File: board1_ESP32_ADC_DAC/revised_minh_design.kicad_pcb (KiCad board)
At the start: 4 copper layers, 94 x 39 mm, 31 parts, among them J1 Conn_01x03_Male, J2 Conn_01x08_Male, J3 Conn_01x08_Male, J4 Conn_01x08_Male, U1 ESP32-DevKit-C, U2 LM7805_TO220, U3 MCP1754S-3302xCB, U4 MCP1825S-3.3V, U5 MCP1501-33xSN, U6 MCP3464R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

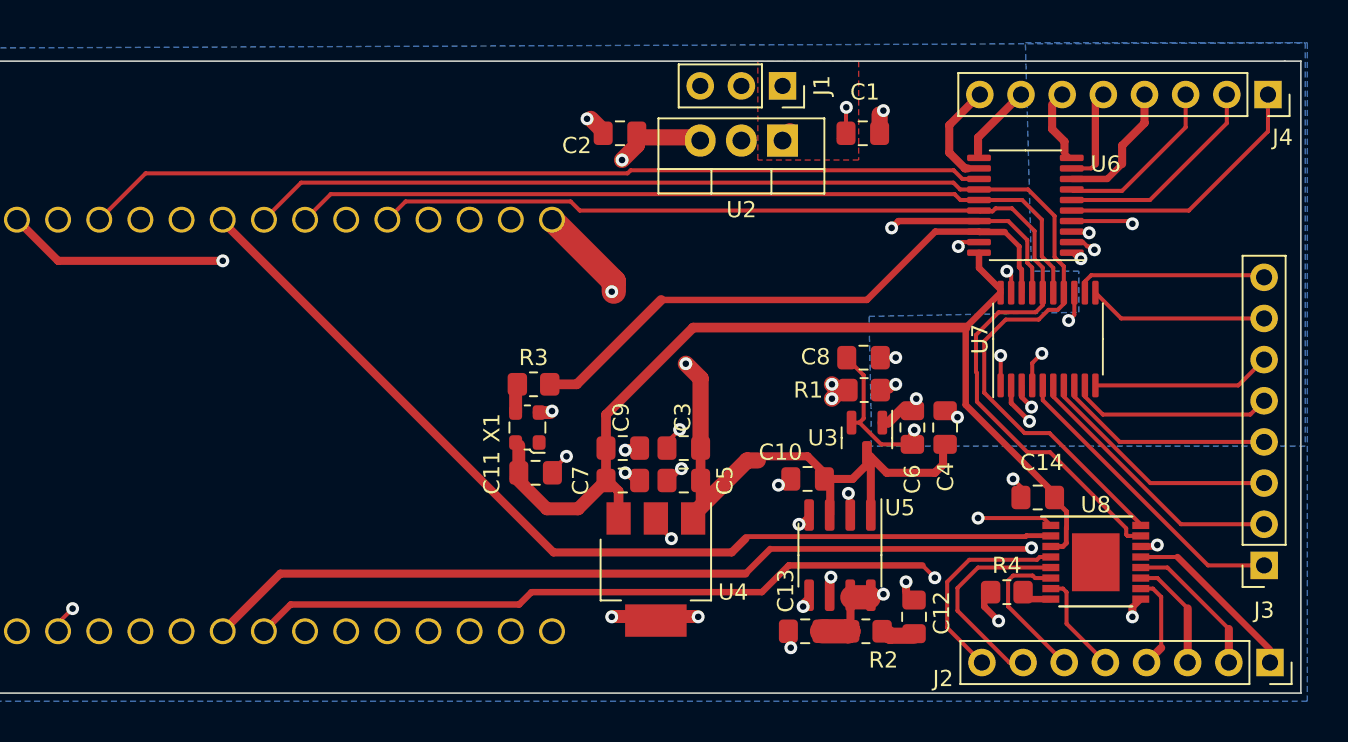
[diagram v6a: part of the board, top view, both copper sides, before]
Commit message: DAC ground to AGND, new AGND polygon pour
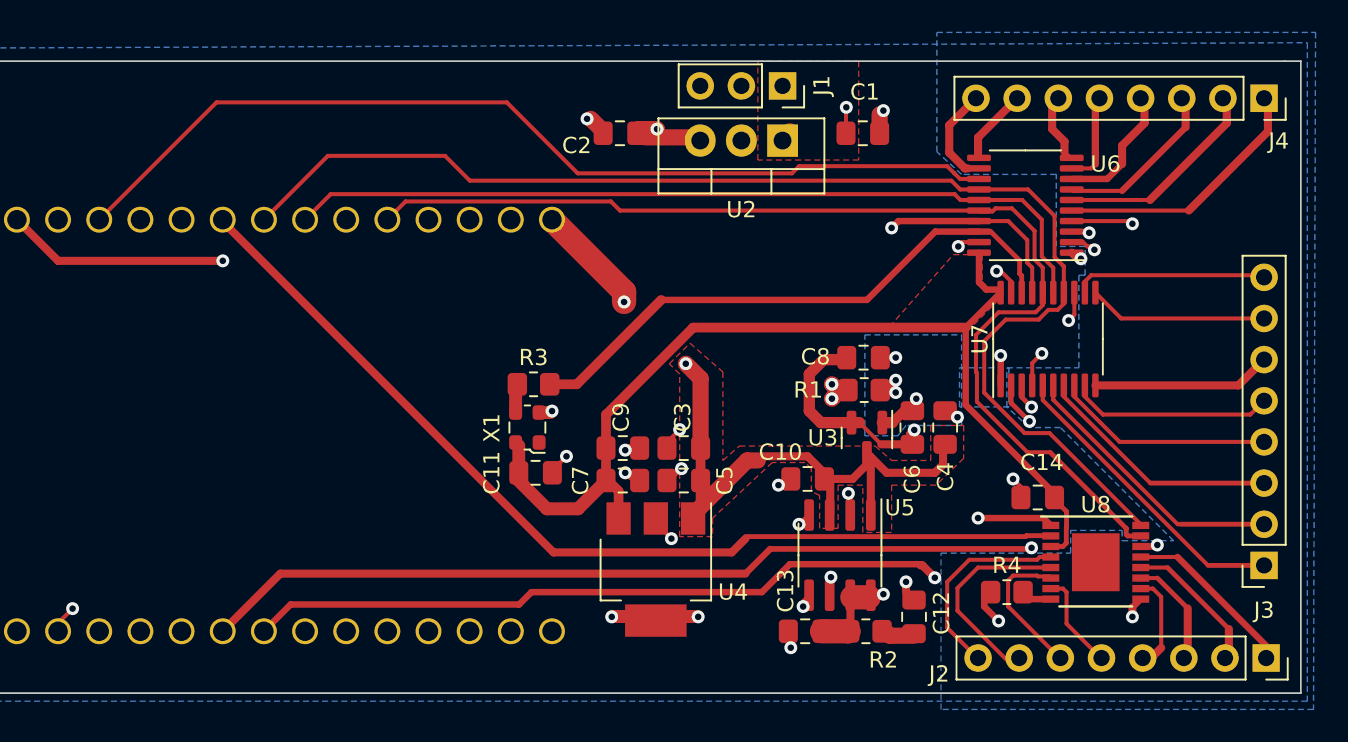
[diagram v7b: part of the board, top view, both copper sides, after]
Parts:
- moved J2 0.37 mm to (141.9, 76.8)
- moved J4 0.33 mm to (141.7, 42.3)
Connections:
- U8 pad 14: Earth -> GNDA
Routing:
- net ~{ADC1_CS}: track 55.8 -> 59.6 mm
- net +3.3VA: track 29.7 -> 33.4 mm
- net +5V: track 60.3 -> 63.9 mm
- net GNDA: track 13.4 -> 15.4 mm, vias 8 -> 10
- net SK: track 78.4 -> 79.8 mm
- net Earth: track 34.1 -> 33.4 mm, vias 25 -> 24
- net +3V3: track 62.5 -> 63.0 mm
- added copper zone on F.Cu, net +3V3
- added copper zone on F.Cu, net +5V

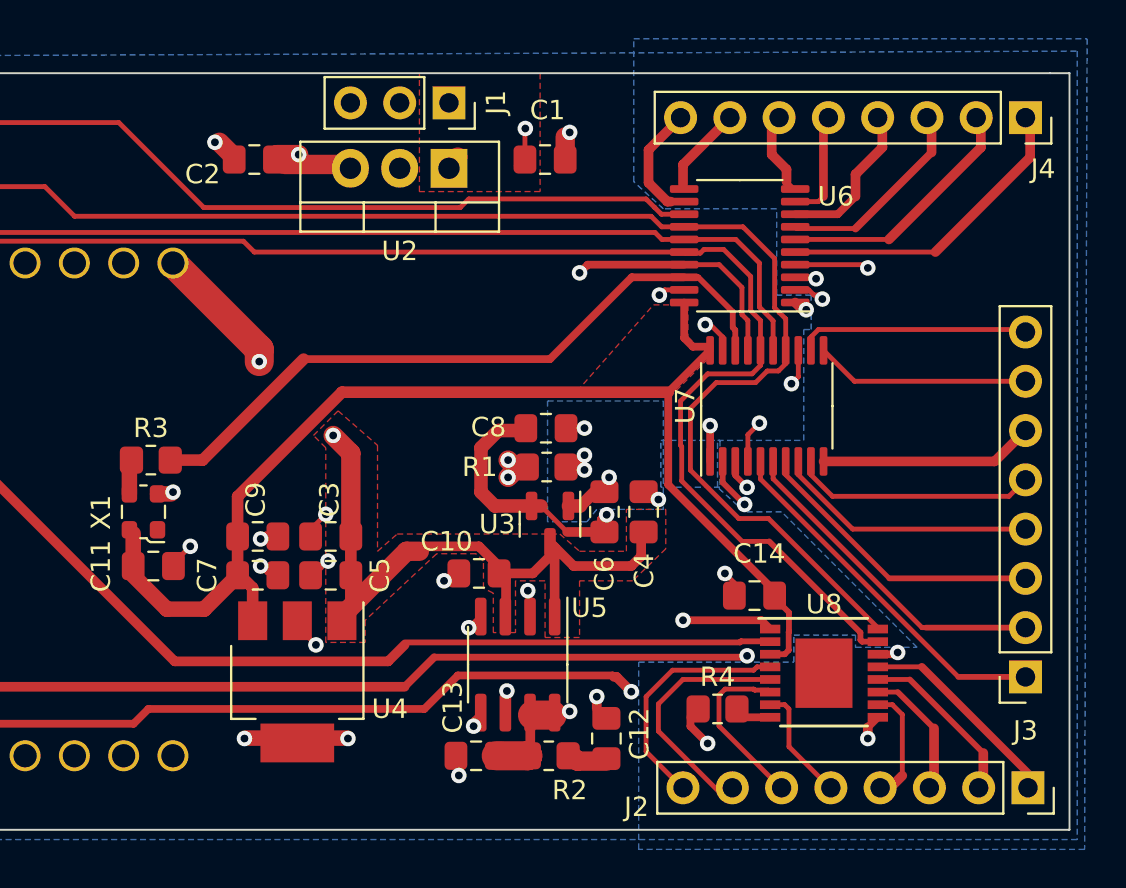
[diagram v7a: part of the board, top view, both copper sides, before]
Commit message: Split ground plane design with no errors
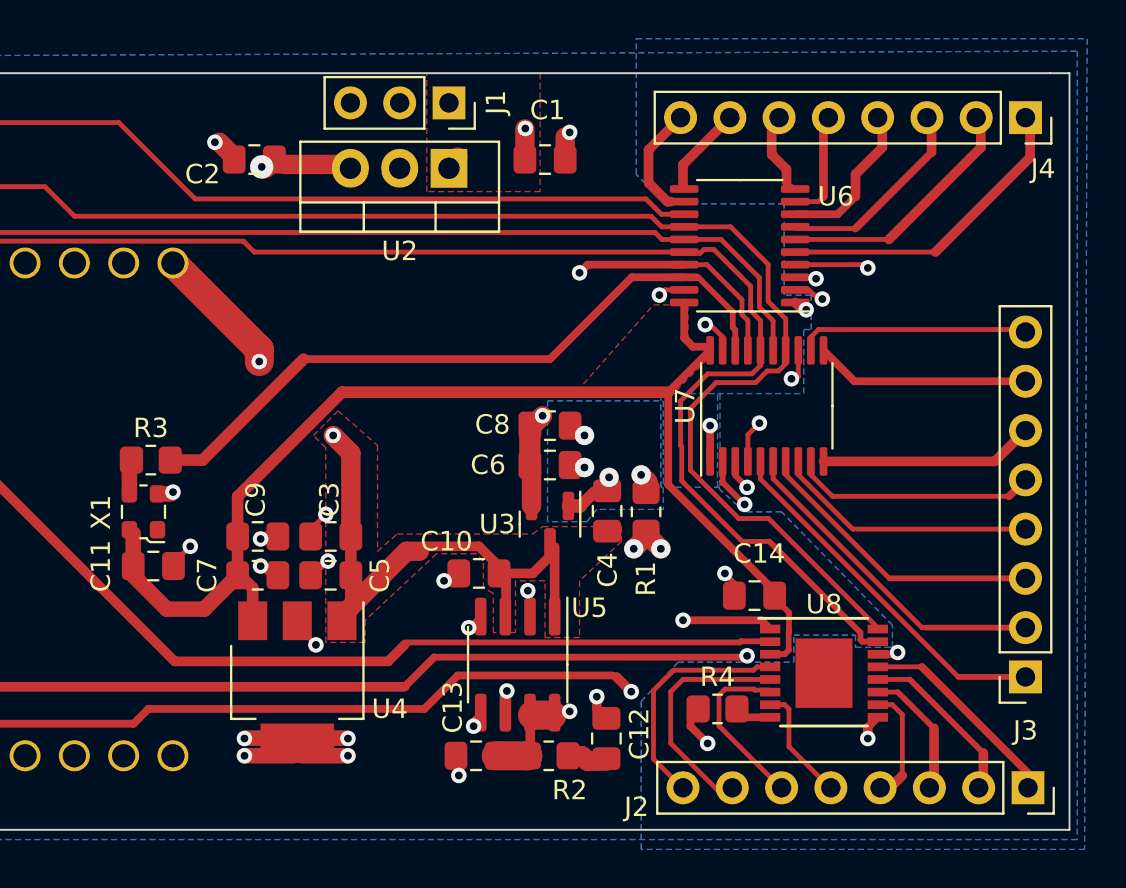
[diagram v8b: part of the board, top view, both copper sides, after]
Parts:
- moved R1 5.62 mm to (122.2, 62.6), turned to 90 degrees
- moved C6 3.70 mm to (117.2, 60.2), turned to 0 degrees
- moved C4 1.88 mm to (120.2, 62.6)
- moved C8 0.25 mm to (117.2, 58.2)
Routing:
- net +5V: track 63.9 -> 54.5 mm
- net Earth: track 33.4 -> 39.9 mm, vias 24 -> 26
- net +3.3VA: track 33.4 -> 27.2 mm
- net GNDA: track 15.4 -> 13.0 mm, vias 10 -> 9
- net ~{ADC2_CS}: track 68.9 -> 66.7 mm
- net ADC1_6: track 4.71 -> 3.84 mm
- net VoutC: track 13.1 -> 12.5 mm
